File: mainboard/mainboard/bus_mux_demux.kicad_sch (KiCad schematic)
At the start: 10 parts, among them IC501 SN74HCS138PWR, IC502 SN74HCS138PWR, IC503 SN74HCS138PWR, IC504 SN74HCS138PWR, IC505 SN74HCS151PWR

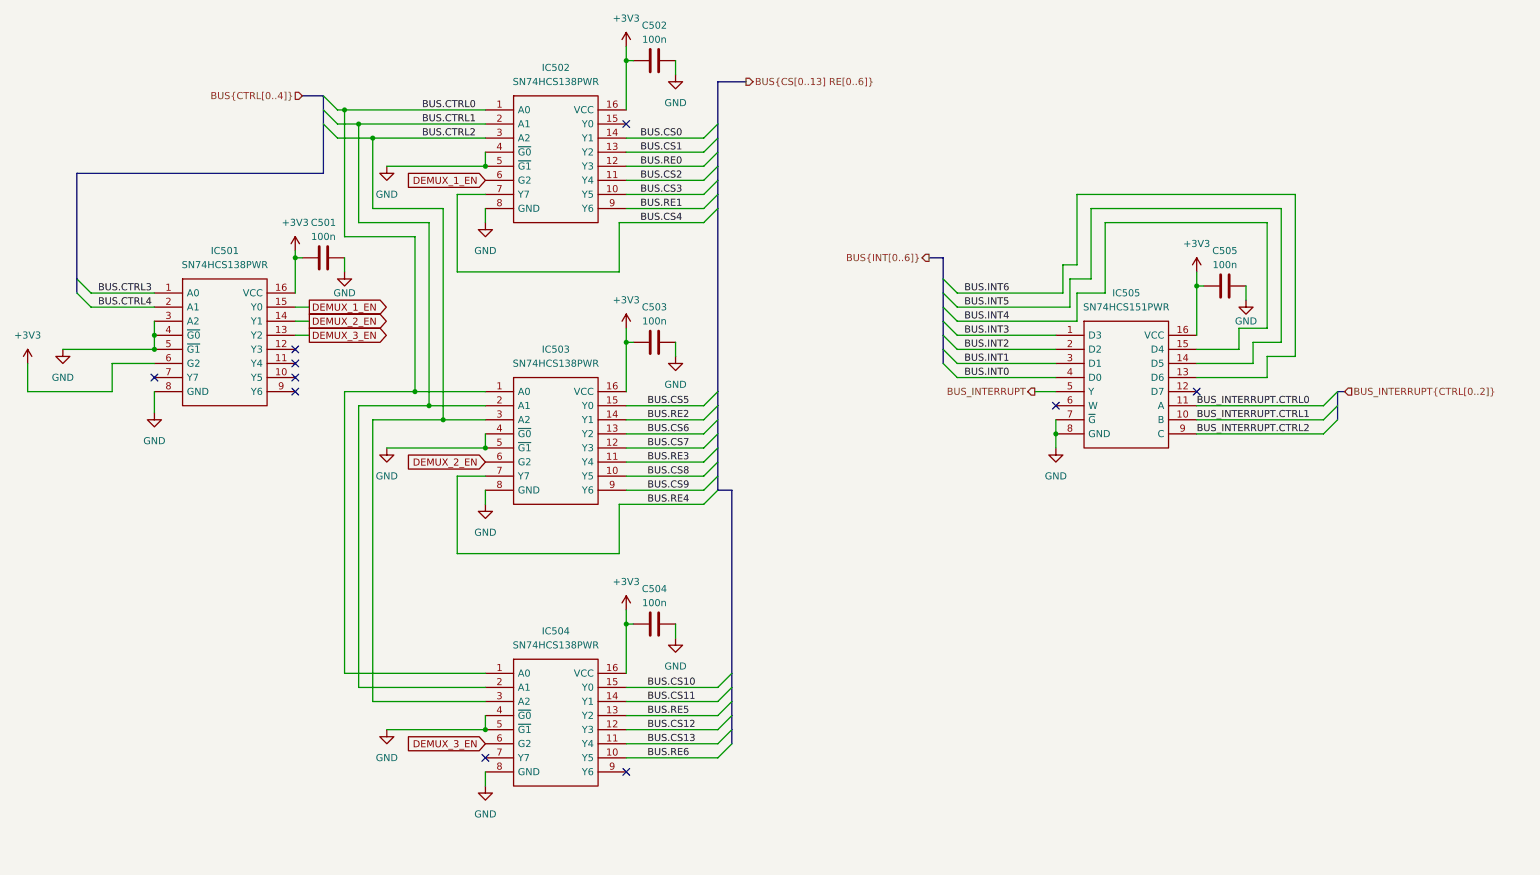
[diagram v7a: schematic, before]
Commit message: gpu and motherboard passes tests, now time for fpga
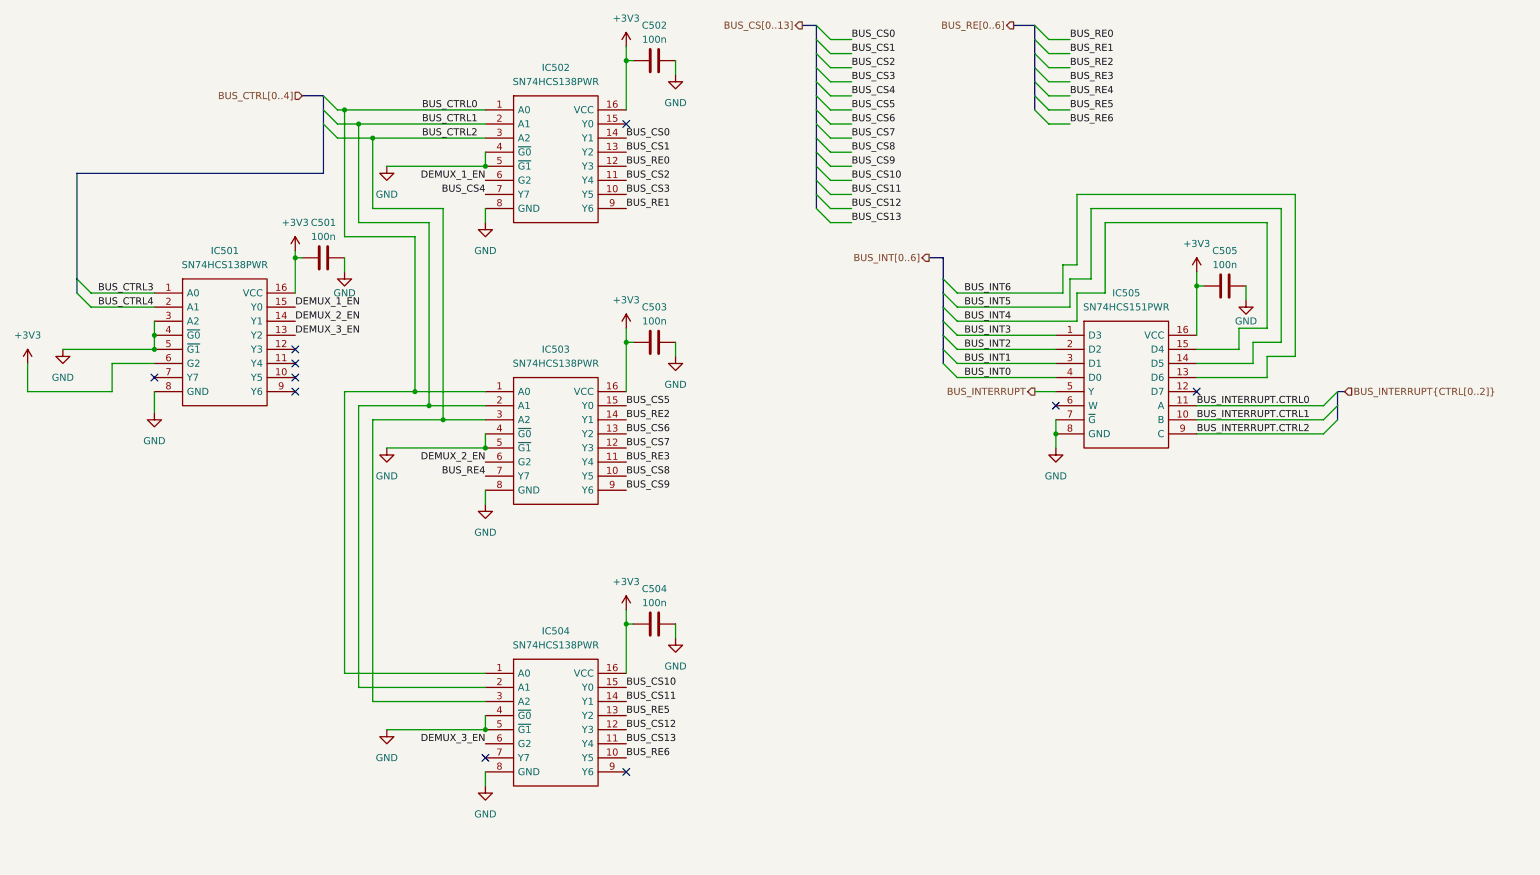
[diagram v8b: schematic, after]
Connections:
- net BUS.CS0 renamed BUS_CS0
- net BUS.CS1 renamed BUS_CS1
- net BUS.CS10 renamed BUS_CS10
- net BUS.CS11 renamed BUS_CS11
- net BUS.CS12 renamed BUS_CS12
- net BUS.CS13 renamed BUS_CS13
- net BUS.CS2 renamed BUS_CS2
- net BUS.CS3 renamed BUS_CS3
- net BUS.CS4 renamed BUS_CS4
- net BUS.CS5 renamed BUS_CS5
- net BUS.CS6 renamed BUS_CS6
- net BUS.CS7 renamed BUS_CS7
- net BUS.CS8 renamed BUS_CS8
- net BUS.CS9 renamed BUS_CS9
- net BUS.CTRL0 renamed BUS_CTRL0
- net BUS.CTRL1 renamed BUS_CTRL1
- net BUS.CTRL2 renamed BUS_CTRL2
- net BUS.CTRL3 renamed BUS_CTRL3
- net BUS.CTRL4 renamed BUS_CTRL4
- net BUS.INT0 renamed BUS_INT0
- net BUS.INT1 renamed BUS_INT1
- net BUS.INT2 renamed BUS_INT2
- net BUS.INT3 renamed BUS_INT3
- net BUS.INT4 renamed BUS_INT4
- net BUS.INT5 renamed BUS_INT5
- net BUS.INT6 renamed BUS_INT6
- net BUS.RE0 renamed BUS_RE0
- net BUS.RE1 renamed BUS_RE1
- net BUS.RE2 renamed BUS_RE2
- net BUS.RE3 renamed BUS_RE3
- net BUS.RE4 renamed BUS_RE4
- net BUS.RE5 renamed BUS_RE5
- net BUS.RE6 renamed BUS_RE6
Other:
- title: (none) -> MSPC
